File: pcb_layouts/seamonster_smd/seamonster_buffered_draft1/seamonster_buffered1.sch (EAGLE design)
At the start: 122 parts, among them IC1 7808DT, IC2 4051D, IC3 4051D, IC4 DG408DY, IC5 4046D, IC6 40106D, IC7 4070D, IC8 4046D, IC9 4040D, Q1 THONKICONNNEW, Q2 THONKICONNNEW, Q3 THONKICONNNEW, Q4 THONKICONNNEW, Q5 THONKICONNNEW, Q6 THONKICONNNEW, SW1 SPDT ON-ON, SW2 SPDT ON-ON, SW3 SPDT ON-ON, SW4 SPDT ON-ON, U1 TL084, U2 TL084, U3 TL084

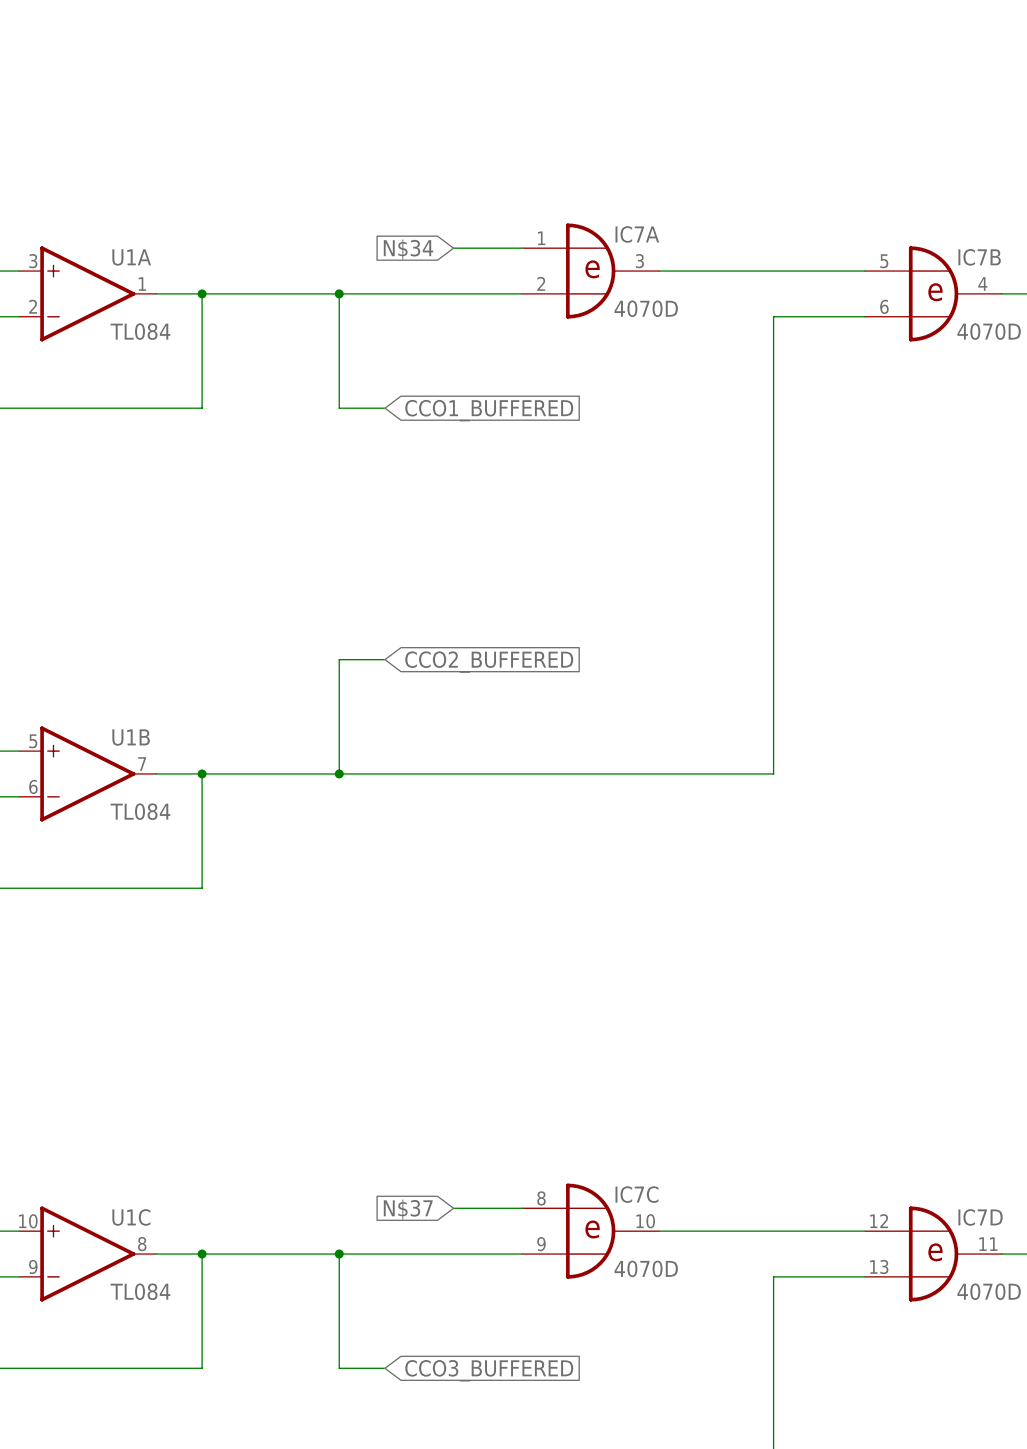
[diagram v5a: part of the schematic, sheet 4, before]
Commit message: routed ABC bus between 4051s, more basic routing
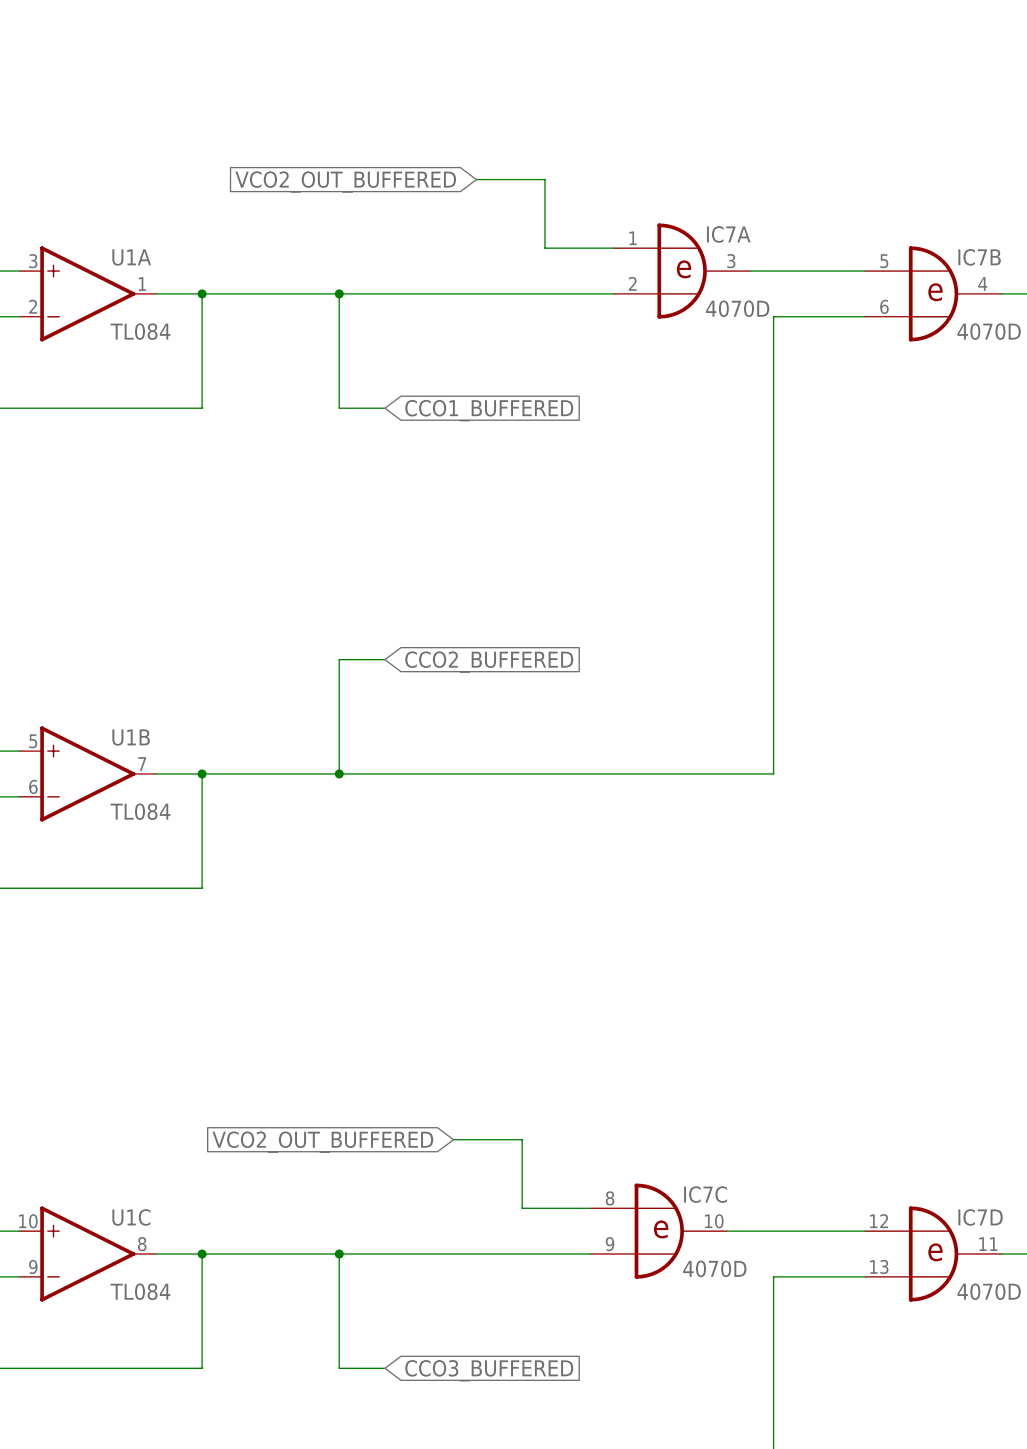
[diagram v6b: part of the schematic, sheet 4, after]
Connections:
- removed net N$34: IC7A.I0
- removed net N$37: IC7C.I0
- net VCO2_OUT_BUFFERED: now also IC7A.I0, IC7C.I0
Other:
- moved on the sheet: IC7A, IC7C
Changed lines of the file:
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@@
 <instance part="IC6" gate="D" x="78.74" y="106.68"/>
 <instance part="IC6" gate="E" x="78.74" y="50.8"/>
-<instance part="IC7" gate="A" x="172.72" y="213.36"/>
+<instance part="IC7" gate="A" x="182.88" y="213.36"/>
 <instance part="IC7" gate="B" x="210.82" y="210.82"/>
-<instance part="IC7" gate="C" x="172.72" y="106.68"/>
+<instance part="IC7" gate="C" x="180.34" y="106.68"/>
 <instance part="IC7" gate="D" x="210.82" y="104.14"/>
 <instance part="SW1" gate="G$1" x="58.42" y="210.82" rot="R90"/>
@@
 <pinref part="IC7" gate="A" pin="I1"/>
 <wire x1="129.54" y1="210.82" x2="144.78" y2="210.82" width="0.1524" layer="91"/>
-<wire x1="144.78" y1="210.82" x2="165.1" y2="210.82" width="0.1524" layer="91"/>
+<wire x1="144.78" y1="210.82" x2="175.26" y2="210.82" width="0.1524" layer="91"/>
 <wire x1="144.78" y1="210.82" x2="144.78" y2="198.12" width="0.1524" layer="91"/>
 <wire x1="144.78" y1="198.12" x2="149.86" y2="198.12" width="0.1524" layer="91"/>
@@
 <pinref part="IC7" gate="C" pin="I1"/>
 <wire x1="129.54" y1="104.14" x2="144.78" y2="104.14" width="0.1524" layer="91"/>
-<wire x1="144.78" y1="104.14" x2="165.1" y2="104.14" width="0.1524" layer="91"/>
+<wire x1="144.78" y1="104.14" x2="172.72" y2="104.14" width="0.1524" layer="91"/>
 <wire x1="144.78" y1="104.14" x2="144.78" y2="91.44" width="0.1524" layer="91"/>
 <wire x1="144.78" y1="91.44" x2="149.86" y2="91.44" width="0.1524" layer="91"/>
@@
 </segment>
 </net>
-<net name="N$34" class="0">
-<segment>
-<pinref part="IC7" gate="A" pin="I0"/>
-<wire x1="165.1" y1="215.9" x2="157.48" y2="215.9" width="0.1524" layer="91"/>
-<label x="157.48" y="215.9" size="1.778" layer="95" rot="R180" xref="yes"/>
-</segment>
-</net>
 <net name="N$35" class="0">
 <segment>
 <pinref part="IC7" gate="A" pin="O"/>
 <pinref part="IC7" gate="B" pin="I0"/>
-<wire x1="180.34" y1="213.36" x2="203.2" y2="213.36" width="0.1524" layer="91"/>
+<wire x1="190.5" y1="213.36" x2="203.2" y2="213.36" width="0.1524" layer="91"/>
 </segment>
 </net>
@@
 <pinref part="IC7" gate="C" pin="O"/>
 <pinref part="IC7" gate="D" pin="I0"/>
-<wire x1="180.34" y1="106.68" x2="203.2" y2="106.68" width="0.1524" layer="91"/>
-</segment>
-</net>
-<net name="N$37" class="0">
-<segment>
-<pinref part="IC7" gate="C" pin="I0"/>
-<wire x1="165.1" y1="109.22" x2="157.48" y2="109.22" width="0.1524" layer="91"/>
-<label x="157.48" y="109.22" size="1.778" layer="95" rot="R180" xref="yes"/>
+<wire x1="187.96" y1="106.68" x2="203.2" y2="106.68" width="0.1524" layer="91"/>
 </segment>
 </net>
@@
 </segment>
 </net>
+<net name="VCO2_OUT_BUFFERED" class="0">
+<segment>
+<pinref part="IC7" gate="C" pin="I0"/>
+<wire x1="172.72" y1="109.22" x2="165.1" y2="109.22" width="0.1524" layer="91"/>
+<wire x1="165.1" y1="109.22" x2="165.1" y2="116.84" width="0.1524" layer="91"/>
+<wire x1="165.1" y1="116.84" x2="157.48" y2="116.84" width="0.1524" layer="91"/>
+<label x="157.48" y="116.84" size="1.778" layer="95" rot="R180" xref="yes"/>
+</segment>
+<segment>
+<pinref part="IC7" gate="A" pin="I0"/>
+<wire x1="175.26" y1="215.9" x2="167.64" y2="215.9" width="0.1524" layer="91"/>
+<wire x1="167.64" y1="215.9" x2="167.64" y2="223.52" width="0.1524" layer="91"/>
+<wire x1="167.64" y1="223.52" x2="160.02" y2="223.52" width="0.1524" layer="91"/>
+<label x="160.02" y="223.52" size="1.778" layer="95" rot="R180" xref="yes"/>
+</segment>
+</net>

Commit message: added jumpers for normalled ABC bus operation
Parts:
- added J1, J2, J3: (no value), SparkFun-Resistors:RESISTOR0805-RES
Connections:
- net N$2 renamed MUX1
- net N$3 renamed MUX2
- net N$4 renamed MUX3
- net N$5 renamed MUX4
- net N$6 renamed MUX5
- net N$7 renamed MUX6
- net N$8 renamed MUX7
- net N$9 renamed MUX8
- new net N$34: A.SWITCH, J1.1
- new net N$37: B.SWITCH, J2.1
- new net N$76: C.SWITCH, J3.1
- net Q1: now also J1.2
- net Q2: now also J2.2
- net Q3: now also J3.2
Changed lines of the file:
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@@
 <part name="GND73" library="supply1" library_urn="urn:adsk.eagle:library:371" deviceset="GND" device=""/>
 <part name="IC1" library="linear" library_urn="urn:adsk.eagle:library:262" deviceset="78*" device="DT" technology="08"/>
+<part name="J1" library="SparkFun-Resistors" deviceset="RESISTOR" device="0805-RES"/>
+<part name="J2" library="SparkFun-Resistors" deviceset="RESISTOR" device="0805-RES"/>
+<part name="J3" library="SparkFun-Resistors" deviceset="RESISTOR" device="0805-RES"/>
 </parts>
 <sheets>
@@
 <instance part="SUPPLY17" gate="G$1" x="284.48" y="91.44"/>
 <instance part="GND73" gate="1" x="251.46" y="218.44"/>
+<instance part="J1" gate="G$1" x="132.08" y="68.58"/>
+<instance part="J2" gate="G$1" x="132.08" y="55.88"/>
+<instance part="J3" gate="G$1" x="132.08" y="43.18"/>
 </instances>
 <busses>
 </busses>
 <nets>
-<net name="N$2" class="0">
+<net name="MUX1" class="0">
 <segment>
 <pinref part="MUX1" gate="G$1" pin="TIP"/>
@@
 </segment>
 </net>
-<net name="N$3" class="0">
+<net name="MUX2" class="0">
 <segment>
 <pinref part="MUX2" gate="G$1" pin="TIP"/>
@@
 </segment>
 </net>
-<net name="N$4" class="0">
+<net name="MUX3" class="0">
 <segment>
 <pinref part="MUX3" gate="G$1" pin="TIP"/>
@@
 </segment>
 </net>
-<net name="N$5" class="0">
+<net name="MUX4" class="0">
 <segment>
 <pinref part="MUX4" gate="G$1" pin="TIP"/>
@@
 </segment>
 </net>
-<net name="N$6" class="0">
+<net name="MUX5" class="0">
 <segment>
 <pinref part="MUX5" gate="G$1" pin="TIP"/>
@@
 </segment>
 </net>
-<net name="N$7" class="0">
+<net name="MUX6" class="0">
 <segment>
 <pinref part="MUX6" gate="G$1" pin="TIP"/>
@@
 </segment>
 </net>
-<net name="N$8" class="0">
+<net name="MUX7" class="0">
 <segment>
 <pinref part="MUX7" gate="G$1" pin="TIP"/>
@@
 </segment>
 </net>
-<net name="N$9" class="0">
+<net name="MUX8" class="0">
 <segment>
 <pinref part="MUX8" gate="G$1" pin="TIP"/>
@@
 </segment>
 </net>
+<net name="N$34" class="0">
+<segment>
+<pinref part="A" gate="G$1" pin="SWITCH"/>
+<pinref part="J1" gate="G$1" pin="1"/>
+<wire x1="101.6" y1="68.58" x2="127" y2="68.58" width="0.1524" layer="91"/>
+</segment>
+</net>
+<net name="N$37" class="0">
+<segment>
+<pinref part="B" gate="G$1" pin="SWITCH"/>
+<pinref part="J2" gate="G$1" pin="1"/>
+<wire x1="101.6" y1="55.88" x2="127" y2="55.88" width="0.1524" layer="91"/>
+</segment>
+</net>
+<net name="N$76" class="0">
+<segment>
+<pinref part="C" gate="G$1" pin="SWITCH"/>
+<pinref part="J3" gate="G$1" pin="1"/>
+<wire x1="101.6" y1="43.18" x2="127" y2="43.18" width="0.1524" layer="91"/>
+</segment>
+</net>
+<net name="Q1" class="0">
+<segment>
+<pinref part="J1" gate="G$1" pin="2"/>
+<wire x1="137.16" y1="68.58" x2="147.32" y2="68.58" width="0.1524" layer="91"/>
+<label x="147.32" y="68.58" size="1.778" layer="95" xref="yes"/>
+</segment>
+</net>
+<net name="Q2" class="0">
+<segment>
+<pinref part="J2" gate="G$1" pin="2"/>
+<wire x1="137.16" y1="55.88" x2="147.32" y2="55.88" width="0.1524" layer="91"/>
+<label x="147.32" y="55.88" size="1.778" layer="95" xref="yes"/>
+</segment>
+</net>
+<net name="Q3" class="0">
+<segment>
+<pinref part="J3" gate="G$1" pin="2"/>
+<wire x1="137.16" y1="43.18" x2="147.32" y2="43.18" width="0.1524" layer="91"/>
+<label x="147.32" y="43.18" size="1.778" layer="95" xref="yes"/>
+</segment>
+</net>
